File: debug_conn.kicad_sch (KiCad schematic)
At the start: 16 parts, among them CN1 HX JN1.27-2X5P ZZ H4.9, J3 Conn_01x06_Pin, U14 TXU0202DCUR

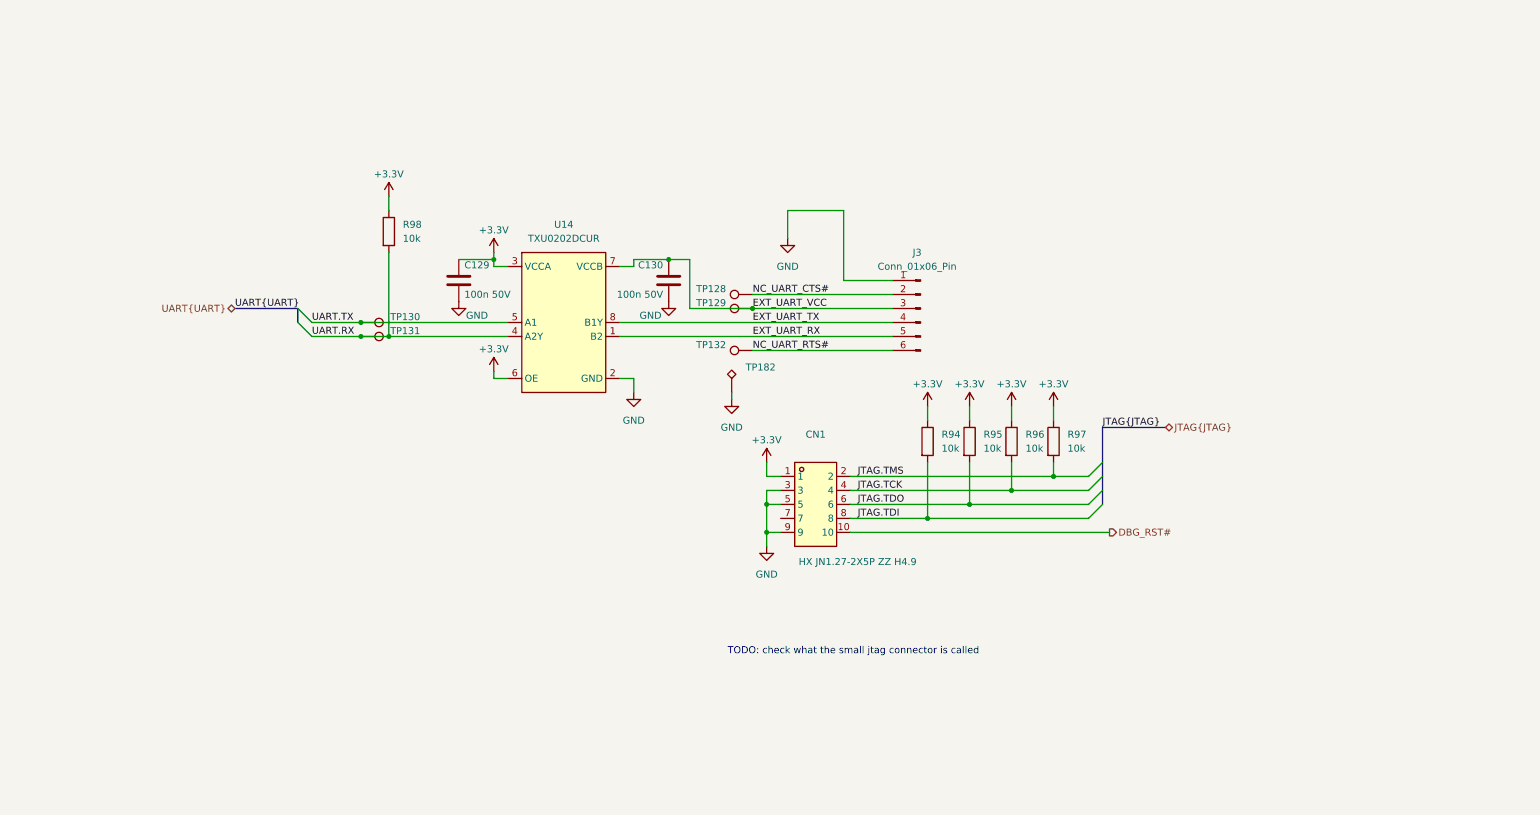
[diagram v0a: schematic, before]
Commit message: fixed some issues, preliminary layout on adc input filter/scaling
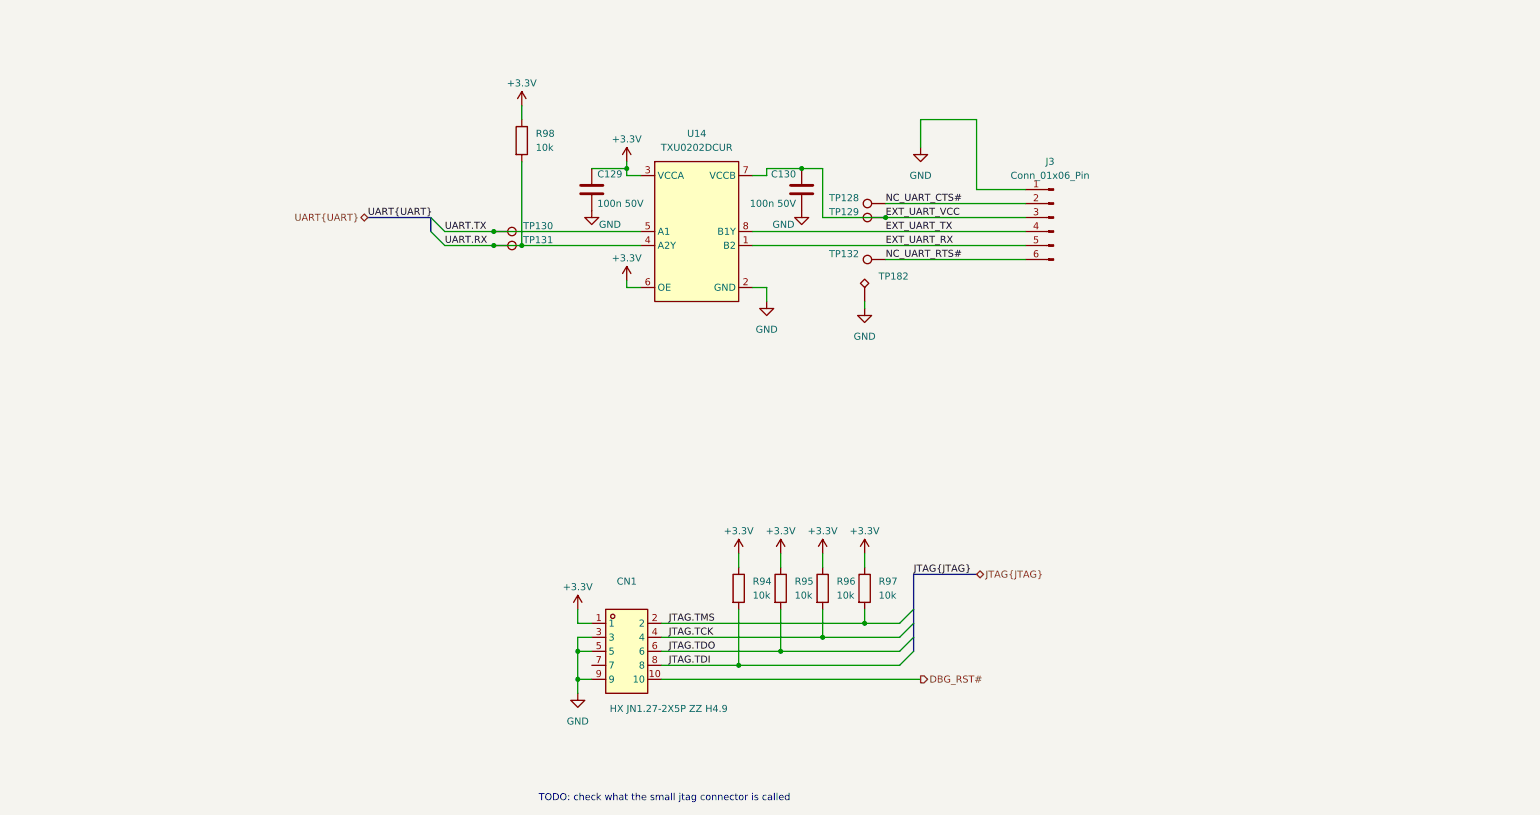
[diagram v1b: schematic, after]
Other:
- moved on the sheet: C129, C130, CN1, J3, R94, R95, R96, R97, R98, TP128, TP129, TP130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

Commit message: did stuff
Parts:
- added C270, C271: 1u 50V, Capacitor_SMD:C_0603_1608Metric, symbol Device:C
- added TP216: TestPoint, TestPoint:TestPoint_THTPad_D1.0mm_Drill0.5mm, symbol Connector:TestPoint
- added U26: TLV77012PDBVR, TLV770:SOT-23-5_DBV_TEX, symbol TLV770:TLV77012PDBVR
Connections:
- net EXT_UART_VCC: now also C270.1, U26.1 (IN), U26.3 (EN); no longer C130.1, U14.7 (VCCB)
- net GND: now also C270.2, C271.2, U26.2 (GND)
- new net +3.3V_UART_CONN: C130.1, C271.1, TP216.1, U14.7 (VCCB), U26.5 (OUT)
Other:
- note added: "Debug JTAG Connector"
- note added: "Debug UART Connector"
- note removed: "TODO: check what the small jtag connector is called"
- moved on the sheet: C129, C130, CN1, J3, R94, R95, R96, R97, R98, TP128, TP129, TP130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

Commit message: did stuff
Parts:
- added R249, R250: 200, Resistor_SMD:R_0603_1608Metric, symbol Device:R
- J3: LCSC missing (none) -> y
- U26: value TLV77012PDBVR -> TLV77033PDBVR
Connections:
- net EXT_UART_TX: now also R250.1; no longer U14.8 (B1Y)
- net UART.RX: now also R249.2; no longer U14.4 (A2Y)
- new net EXT_UART_TX_SHFT: R250.2, U14.8 (B1Y)
- new net UART_RX_SHFT: R249.1, U14.4 (A2Y)
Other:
- moved on the sheet: R98, TP130, TP131

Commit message: fixed a lot of review comments
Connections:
- net EXT_UART_RX: now also J3.4 (Pin_4); no longer J3.5 (Pin_5)
- net EXT_UART_TX: now also J3.5 (Pin_5); no longer J3.4 (Pin_4)
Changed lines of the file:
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@@
+		)
+	)
+	(text_box "Design Note:\nTX/RX naming is from MCU perspective"
+		(exclude_from_sim no)
+		(at 221.615 67.945 0)
+		(size 52.07 11.43)
+		(margins 0.9525 0.9525 0.9525 0.9525)
+		(stroke
+			(width -0.0001)
+			(type solid)
+		)
+		(fill
+			(type none)
+		)
+		(effects
+			(font
+				(size 1.27 1.27)
+			)
+			(justify left top)
 		)
 	)
@@
 	(wire
 		(pts
+			(xy 162.56 64.77) (xy 208.28 64.77)
+		)
+		(stroke
+			(width 0)
+			(type default)
+		)
+	)
+	(wire
+		(pts
 			(xy 143.51 132.08) (xy 143.51 142.24)
 		)
@@
 	(wire
 		(pts
+			(xy 160.02 64.77) (xy 160.02 67.31)
+		)
+		(stroke
+			(width 0)
+			(type default)
+		)
+	)
+	(wire
+		(pts
 			(xy 199.39 54.61) (xy 199.39 41.91)
 		)
@@
 	(wire
 		(pts
-			(xy 149.86 62.23) (xy 208.28 62.23)
+			(xy 149.86 62.23) (xy 162.56 62.23)
 		)
 		(stroke
@@
 	(wire
 		(pts
+			(xy 162.56 62.23) (xy 162.56 64.77)
+		)
+		(stroke
+			(width 0)
+			(type default)
+		)
+	)
+	(wire
+		(pts
 			(xy 182.88 59.69) (xy 208.28 59.69)
 		)
@@
 	(wire
 		(pts
+			(xy 165.1 67.31) (xy 165.1 62.23)
+		)
+		(stroke
+			(width 0)
+			(type default)
+		)
+	)
+	(wire
+		(pts
 			(xy 44.45 64.77) (xy 53.34 64.77)
 		)
@@
 	(wire
 		(pts
-			(xy 114.3 64.77) (xy 208.28 64.77)
+			(xy 114.3 64.77) (xy 160.02 64.77)
 		)
 		(stroke
@@
 	(wire
 		(pts
+			(xy 165.1 62.23) (xy 208.28 62.23)
+		)
+		(stroke
+			(width 0)
+			(type default)
+		)
+	)
+	(wire
+		(pts
 			(xy 58.42 39.37) (xy 58.42 41.91)
 		)
@@
 		(pts
 			(xy 91.44 50.8) (xy 91.44 52.07)
+		)
+		(stroke
+			(width 0)
+			(type default)
+		)
+	)
+	(wire
+		(pts
+			(xy 160.02 67.31) (xy 165.1 67.31)
 		)
 		(stroke
@@
 		)
 	)
-	(label "EXT_UART_RX"
+	(label "EXT_UART_TX"
 		(at 182.88 64.77 0)
 		(effects
@@
 		)
 	)
-	(label "EXT_UART_TX"
+	(label "EXT_UART_RX"
 		(at 182.88 62.23 0)
 		(effects

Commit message: pre-changing properties
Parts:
- R249, R250: footprint Resistor_SMD:R_0603_1608Metric -> Resistor_SMD:R_0402_1005Metric; LCSC missing (none) -> n; MPN (none) -> 0402WGF2000TCE; Manufacturer (none) -> UNI-ROYAL(Uniroyal Elec); Power (none) -> 62.5mW; Tolerance (none) -> 1%; Voltage (none) -> 50V
- R94, R95, R96, R97, R98: LCSC Basic/Pref x -> y; LCSC missing (none) -> n; MPN (none) -> 0402WGF1002TCE; Manufacturer (none) -> UNI-ROYAL; Power (none) -> 62.5mW; Tolerance (none) -> 1%
